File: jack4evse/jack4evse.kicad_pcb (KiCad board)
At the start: 2 copper layers, 24.8 x 87.1 mm, 10 parts, among them J1 Conn_02x08_Odd_Even, J2 Conn_01x04, J3 Conn_01x04, J4 Conn_02x08_Odd_Even, J5 Conn_01x04, J6 Conn_01x04

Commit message: jack/pcb: Done routing
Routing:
- net /R1: track 0.00 -> 94.8 mm, vias 0 -> 5
- net /G1: track 0.00 -> 93.9 mm, vias 0 -> 5
- net /R2: track 0.00 -> 92.8 mm, vias 0 -> 2
- net /B1: track 0.00 -> 92.6 mm, vias 0 -> 5
- net /G2: track 0.00 -> 92.5 mm, vias 0 -> 2
- net /B2: track 0.00 -> 91.5 mm, vias 0 -> 2
- net +5V: track 83.7 -> 174.2 mm, vias 4 -> 6
- net /R3: track 0.00 -> 89.7 mm, vias 0 -> 2
- net /G3: track 0.00 -> 89.3 mm, vias 0 -> 2
- net /B3: track 0.00 -> 89.0 mm, vias 0 -> 2
- net /B0: track 79.0 -> 92.4 mm, vias 6 -> 7
- net /G0: track 77.7 -> 89.8 mm, vias 4 -> 5

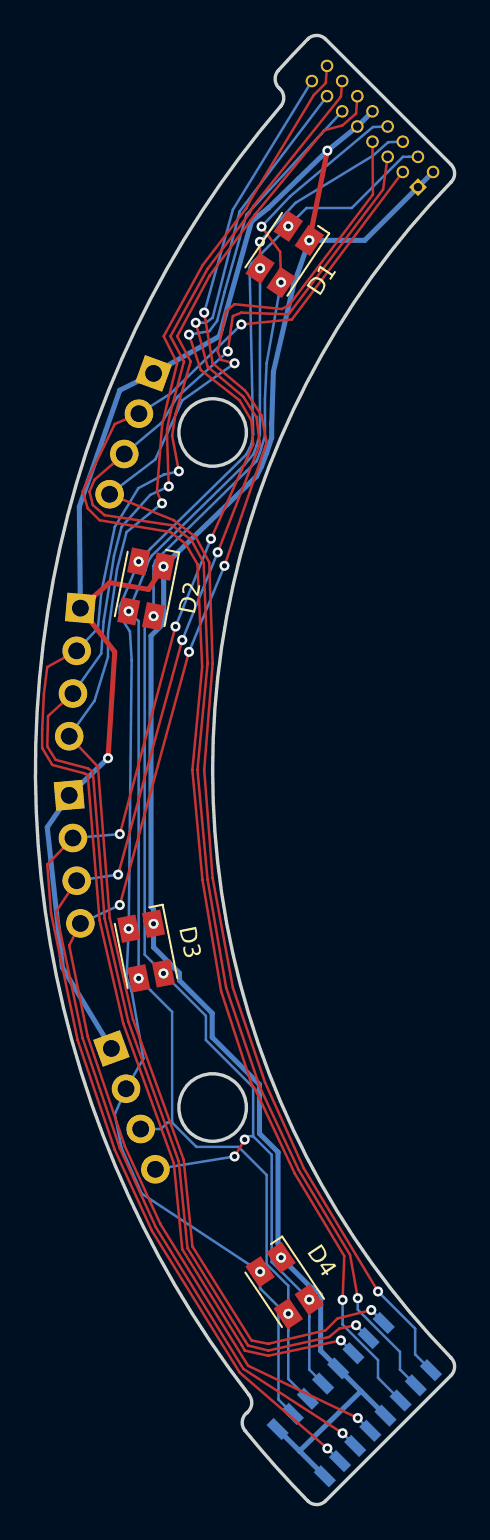
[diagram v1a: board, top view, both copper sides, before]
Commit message: jack: Re-route board with new connector and new board outline
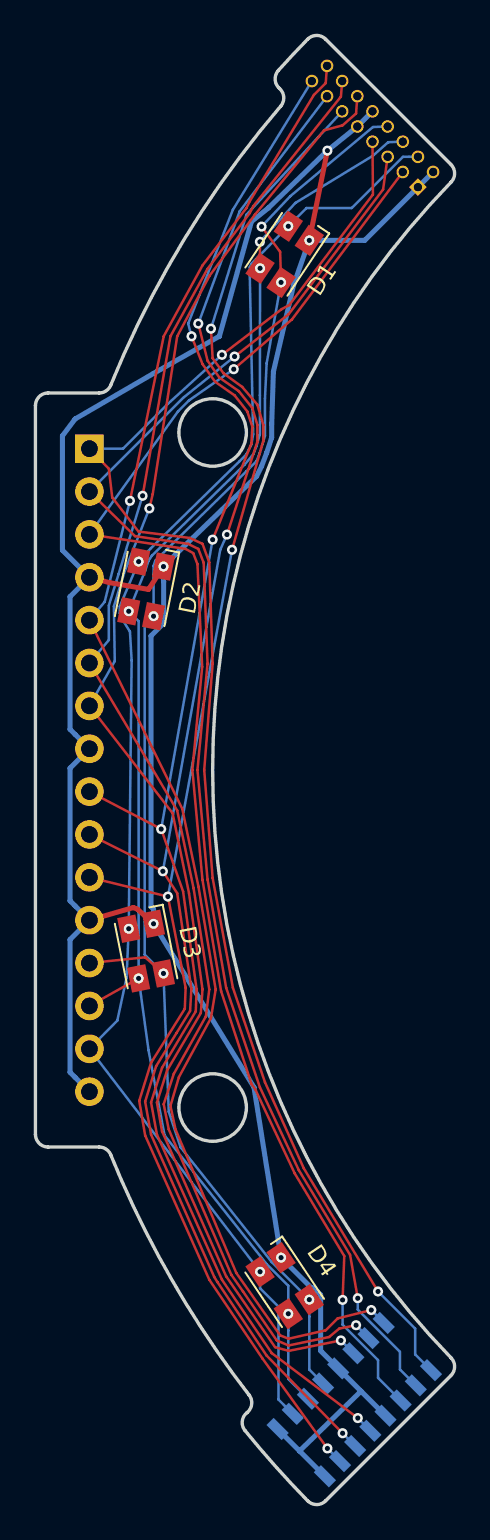
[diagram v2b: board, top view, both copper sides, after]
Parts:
- removed J3, J5, J6: Conn_01x04, Connector_PinHeader_2.54mm:PinHeader_1x04_P2.54mm_Horizontal
- J2: value Conn_01x04 -> Conn_01x16; footprint Connector_PinHeader_2.54mm:PinHeader_1x04_P2.54mm_Horizontal -> Connector_PinHeader_2.54mm:PinHeader_1x16_P2.54mm_Horizontal
- moved J2 35.6 mm to (122.7, 91.0), turned to 180 degrees
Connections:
- J2 pad 1: +5V -> /B3
- J2 pad 2: /R0 -> /G3
- J2 pad 3: /G0 -> /R3
- J2 pad 4: /B0 -> +5V
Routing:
- net +5V: track 174.2 -> 180.5 mm, vias 6 -> 5
- net /R2: track 92.8 -> 88.3 mm
- net /G2: track 92.5 -> 88.7 mm
- net /B0: track 92.4 -> 90.0 mm, vias 7 -> 5
- net /B2: track 91.5 -> 89.3 mm
- net /G3: track 89.3 -> 87.6 mm
- net /R1: track 94.8 -> 93.2 mm, vias 5 -> 4
- net /B1: track 92.6 -> 94.2 mm, vias 5 -> 4
- net /R3: track 89.7 -> 88.4 mm
- net /G0: track 89.8 -> 88.8 mm
- net /G1: track 93.9 -> 93.8 mm, vias 5 -> 4
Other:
- outline, holes or cut-outs redrawn
- net class Power added: clearance 0.15, trace_width 0.3, via_dia 0.6, via_drill 0.3

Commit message: jack: Change LED footprint to ma ones
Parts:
- D1, D2, D3, D4: footprint LED_SMD:LED_Avago_PLCC4_3.2x2.8mm_CW -> ma4evse:LED_Avago_PLCC4_3.2x2.8mm_CW

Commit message: jack/pcb: Add enexten logo + rev info to silkscreen
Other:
- board text added: "Dalton EVSE "Jack" board rev 1.0 (c) Tuetuopay 2019"
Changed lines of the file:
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@@
   (general
     (thickness 1.6)
-    (drawings 24)
+    (drawings 25)
     (tracks 394)
     (zones 0)
-    (modules 7)
+    (modules 8)
     (nets 14)
   )
@@
     )
   )
+  (gr_text "Dalton EVSE\n\"Jack\" board rev 1.0\n(c) Tuetuopay 2019" (at 126.5 104 90) (layer B.SilkS)
+    (effects (font (size 1 1) (thickness 0.15)) (justify left mirror))
+  )
   (gr_arc (start 123.268929 86.910001) (end 123.268929 87.660001) (angle -67.85329534) (layer Edge.Cuts) (width 0.2))
   (gr_line (start 136.693544 153.306457) (end 144.11825 145.88175) (layer Edge.Cuts) (width 0.2))
@@
   (gr_arc (start 123.268929 133.089999) (end 123.963595 132.807264) (angle -67.85416667) (layer Edge.Cuts) (width 0.2))
   (gr_line (start 120.25 87.660001) (end 123.268929 87.660001) (layer Edge.Cuts) (width 0.2))
-  (via (at 134.055064 81.106965) (size 0.6) (drill 0.3) (layers F.Cu B.Cu) (net 3))
-  (via (at 126.498352 100.887915) (size 0.6) (drill 0.3) (layers F.Cu B.Cu) (net 3))
-  (via (at 127.08619 122.053929) (size 0.6) (drill 0.3) (layers F.Cu B.Cu) (net 3))
-  (via (at 135.728299 141.383072) (size 0.6) (drill 0.3) (layers F.Cu B.Cu) (net 3))
-  (via (at 135.728299 78.616928) (size 0.6) (drill 0.3) (layers F.Cu B.Cu) (net 4))
-  (via (at 127.08619 97.946071) (size 0.6) (drill 0.3) (layers F.Cu B.Cu) (net 4))
-  (via (at 126.498352 119.112085) (size 0.6) (drill 0.3) (layers F.Cu B.Cu) (net 4))
-  (via (at 134.055064 138.893035) (size 0.6) (drill 0.3) (layers F.Cu B.Cu) (net 4))
   (via (at 134.48328 77.780311) (size 0.6) (drill 0.3) (layers F.Cu B.Cu) (net 1))
   (via (at 125.615268 97.652151) (size 0.6) (drill 0.3) (layers F.Cu B.Cu) (net 1))
@@
   (segment (start 132.810045 139.729652) (end 132.810045 140.710045) (width 0.15) (layer B.Cu) (net 1))
   (segment (start 132.810045 140.710045) (end 133.9 141.8) (width 0.15) (layer B.Cu) (net 1))
-  (via (at 132.810045 80.270348) (size 0.6) (drill 0.3) (layers F.Cu B.Cu) (net 2))
-  (via (at 125.02743 100.593995) (size 0.6) (drill 0.3) (layers F.Cu B.Cu) (net 2))
   (via (at 125.02743 119.406005) (size 0.6) (drill 0.3) (layers F.Cu B.Cu) (net 1))
   (segment (start 131.6 91.7) (end 132 91.3) (width 0.15) (layer B.Cu) (net 1))
@@
   (segment (start 122.7 126.52) (end 124.35 124.85) (width 0.15) (layer B.Cu) (net 1))
   (segment (start 124.35 124.85) (end 124.9 122.3) (width 0.15) (layer B.Cu) (net 1))
+  (via (at 132.810045 80.270348) (size 0.6) (drill 0.3) (layers F.Cu B.Cu) (net 2))
+  (via (at 125.02743 100.593995) (size 0.6) (drill 0.3) (layers F.Cu B.Cu) (net 2))
   (via (at 125.615268 122.347849) (size 0.6) (drill 0.3) (layers F.Cu B.Cu) (net 2))
   (via (at 134.48328 142.219689) (size 0.6) (drill 0.3) (layers F.Cu B.Cu) (net 2))
@@
   (segment (start 127.15 131.65) (end 126.2 126.6) (width 0.15) (layer B.Cu) (net 2))
   (segment (start 126.2 126.6) (end 125.615268 122.347849) (width 0.15) (layer B.Cu) (net 2))
+  (via (at 134.055064 81.106965) (size 0.6) (drill 0.3) (layers F.Cu B.Cu) (net 3))
+  (via (at 126.498352 100.887915) (size 0.6) (drill 0.3) (layers F.Cu B.Cu) (net 3))
+  (via (at 127.08619 122.053929) (size 0.6) (drill 0.3) (layers F.Cu B.Cu) (net 3))
+  (via (at 135.728299 141.383072) (size 0.6) (drill 0.3) (layers F.Cu B.Cu) (net 3))
   (segment (start 135.728299 142.386673) (end 135.728299 141.383072) (width 0.15) (layer B.Cu) (net 3))
   (segment (start 135.728299 145.528299) (end 135.728299 142.386673) (width 0.15) (layer B.Cu) (net 3))
@@
   (segment (start 128.1 132.35) (end 127.4 130.25) (width 0.15) (layer B.Cu) (net 3))
   (segment (start 127.4 130.25) (end 127.08619 122.053929) (width 0.15) (layer B.Cu) (net 3))
+  (via (at 135.728299 78.616928) (size 0.6) (drill 0.3) (layers F.Cu B.Cu) (net 4))
+  (via (at 127.08619 97.946071) (size 0.6) (drill 0.3) (layers F.Cu B.Cu) (net 4))
+  (via (at 126.498352 119.112085) (size 0.6) (drill 0.3) (layers F.Cu B.Cu) (net 4))
+  (via (at 134.055064 138.893035) (size 0.6) (drill 0.3) (layers F.Cu B.Cu) (net 4))
   (segment (start 126.498352 118.247259) (end 126.348361 118.097268) (width 0.3) (layer B.Cu) (net 4))
   (segment (start 126.498352 119.112085) (end 126.498352 118.247259) (width 0.3) (layer B.Cu) (net 4))

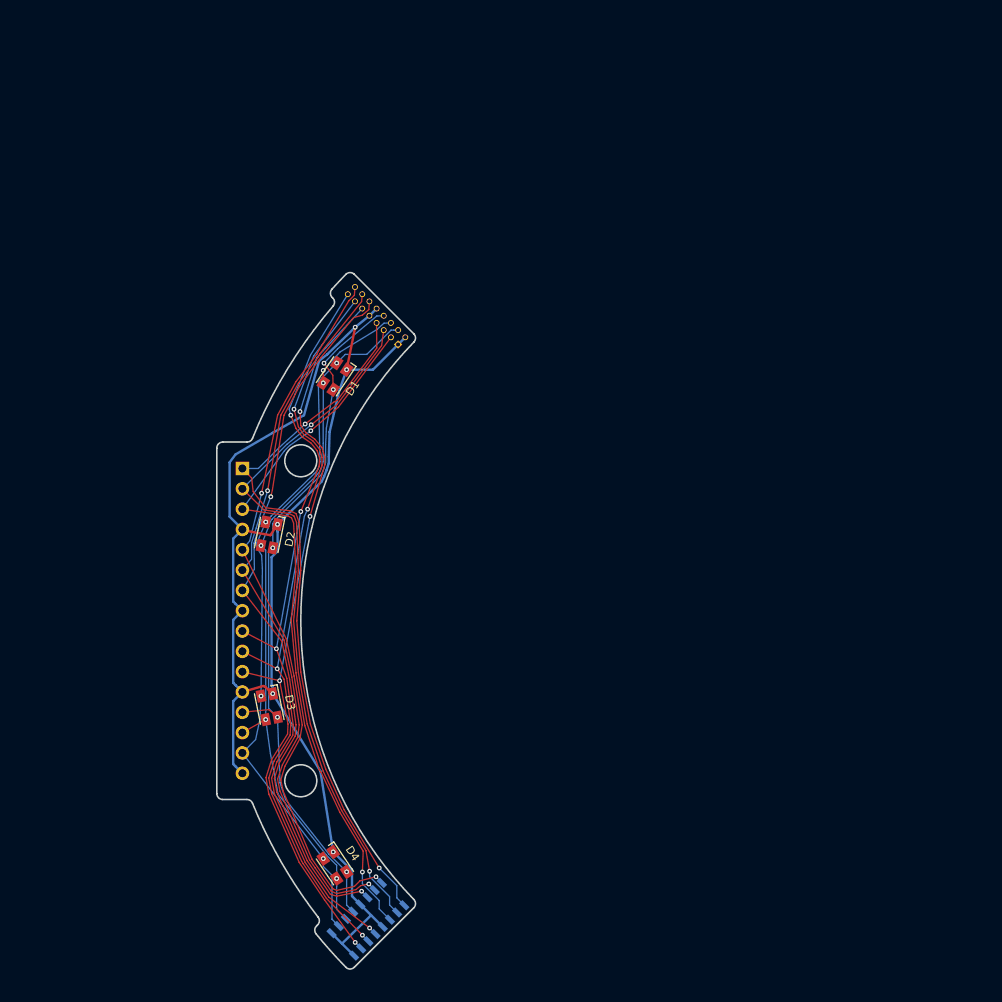
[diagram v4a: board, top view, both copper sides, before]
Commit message: jack/{sch, pcb}: Make one single ring pcb with all leds
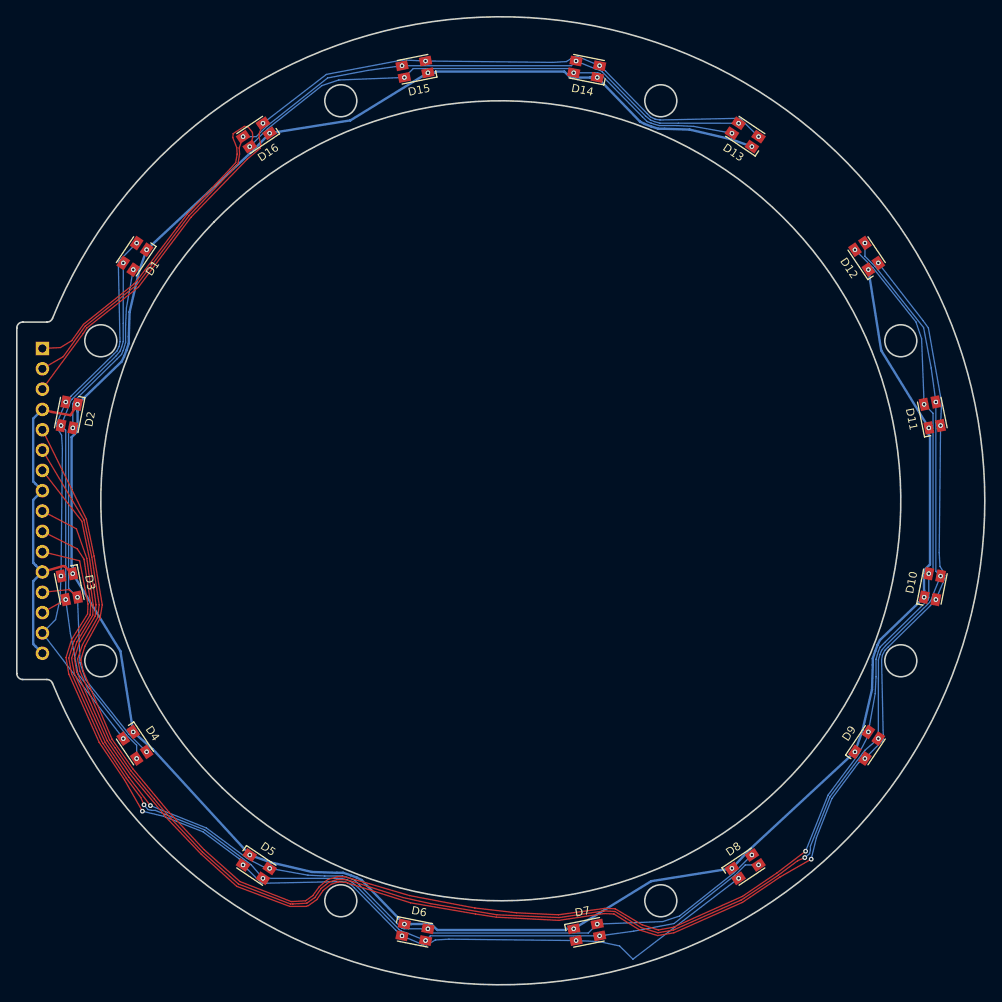
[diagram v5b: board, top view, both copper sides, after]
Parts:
- removed J1: Conn_02x08_Odd_Even, ma4evse:CLP-108-02-F-DH
- removed J4: Conn_02x08_Odd_Even, ma4evse:PinHeader_2x08_P1.27mm_Horizontal
- added D10: ASMB-MTB0-0A3A2, ma4evse:LED_Avago_PLCC4_3.2x2.8mm_CW, F.Cu at (208.9, 105.7)
- added D11: ASMB-MTB0-0A3A2, ma4evse:LED_Avago_PLCC4_3.2x2.8mm_CW, F.Cu at (208.9, 84.3)
- added D12: ASMB-MTB0-0A3A2, ma4evse:LED_Avago_PLCC4_3.2x2.8mm_CW, F.Cu at (200.7, 64.4)
- added D13: ASMB-MTB0-0A3A2, ma4evse:LED_Avago_PLCC4_3.2x2.8mm_CW, F.Cu at (185.6, 49.3)
- added D14: ASMB-MTB0-0A3A2, ma4evse:LED_Avago_PLCC4_3.2x2.8mm_CW, F.Cu at (165.7, 41.1)
- added D15: ASMB-MTB0-0A3A2, ma4evse:LED_Avago_PLCC4_3.2x2.8mm_CW, F.Cu at (144.3, 41.1)
- added D16: ASMB-MTB0-0A3A2, ma4evse:LED_Avago_PLCC4_3.2x2.8mm_CW, F.Cu at (124.4, 49.3)
- added D5: ASMB-MTB0-0A3A2, ma4evse:LED_Avago_PLCC4_3.2x2.8mm_CW, F.Cu at (124.4, 140.7)
- added D6: ASMB-MTB0-0A3A2, ma4evse:LED_Avago_PLCC4_3.2x2.8mm_CW, F.Cu at (144.3, 148.9)
- added D7: ASMB-MTB0-0A3A2, ma4evse:LED_Avago_PLCC4_3.2x2.8mm_CW, F.Cu at (165.7, 148.9)
- added D8: ASMB-MTB0-0A3A2, ma4evse:LED_Avago_PLCC4_3.2x2.8mm_CW, F.Cu at (185.6, 140.7)
- added D9: ASMB-MTB0-0A3A2, ma4evse:LED_Avago_PLCC4_3.2x2.8mm_CW, F.Cu at (200.7, 125.6)
- moved D4 29.2 mm to (109.3, 125.6)
- moved D1 29.2 mm to (109.3, 64.4)
- moved D2 29.2 mm to (101.1, 84.3)
- moved D3 29.2 mm to (101.1, 105.7)
- moved J2 29.2 mm to (97.7, 76.0)
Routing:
- net +5V: track 180.5 -> 367.4 mm, vias 5 -> 16
- net /G2: track 88.7 -> 225.3 mm, vias 2 -> 5
- net /B2: track 89.3 -> 225.3 mm, vias 2 -> 5
- net /R2: track 88.3 -> 221.5 mm, vias 2 -> 5
- net /B1: track 94.2 -> 126.6 mm, vias 4 -> 5
- net /G1: track 93.8 -> 125.9 mm, vias 4 -> 5
- net /R1: track 93.2 -> 124.0 mm, vias 4 -> 5
- net /R3: track 88.4 -> 112.3 mm, vias 2 -> 4
- net /B3: track 88.7 -> 109.5 mm, vias 2 -> 4
- net /G3: track 87.6 -> 107.0 mm, vias 2 -> 4
- net /B0: track 90.0 -> 71.3 mm, vias 5 -> 4
- net /R0: track 88.8 -> 70.2 mm
- net /G0: track 88.8 -> 71.1 mm, vias 5 -> 4
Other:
- board size 24.8 x 87.1 mm -> 121 x 121 mm
- board text added: "Dalton EVSE "Jack" board rev 1.1 (c) Tuetuopay 2019-2020"
- board text removed: "Dalton EVSE "Jack" board rev 1.0 (c) Tuetuopay 2019"
